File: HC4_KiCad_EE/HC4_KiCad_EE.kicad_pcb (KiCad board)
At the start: 2 copper layers, 100 x 100 mm, 124 parts, among them IC1 74HC86, IC10 74HC161, IC11 74HC02, IC12 74HC00, IC13 74HC4053, IC14 74HC74, IC15 74HC14, IC2 74HC283, IC3 74HC253, IC4 74HC253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

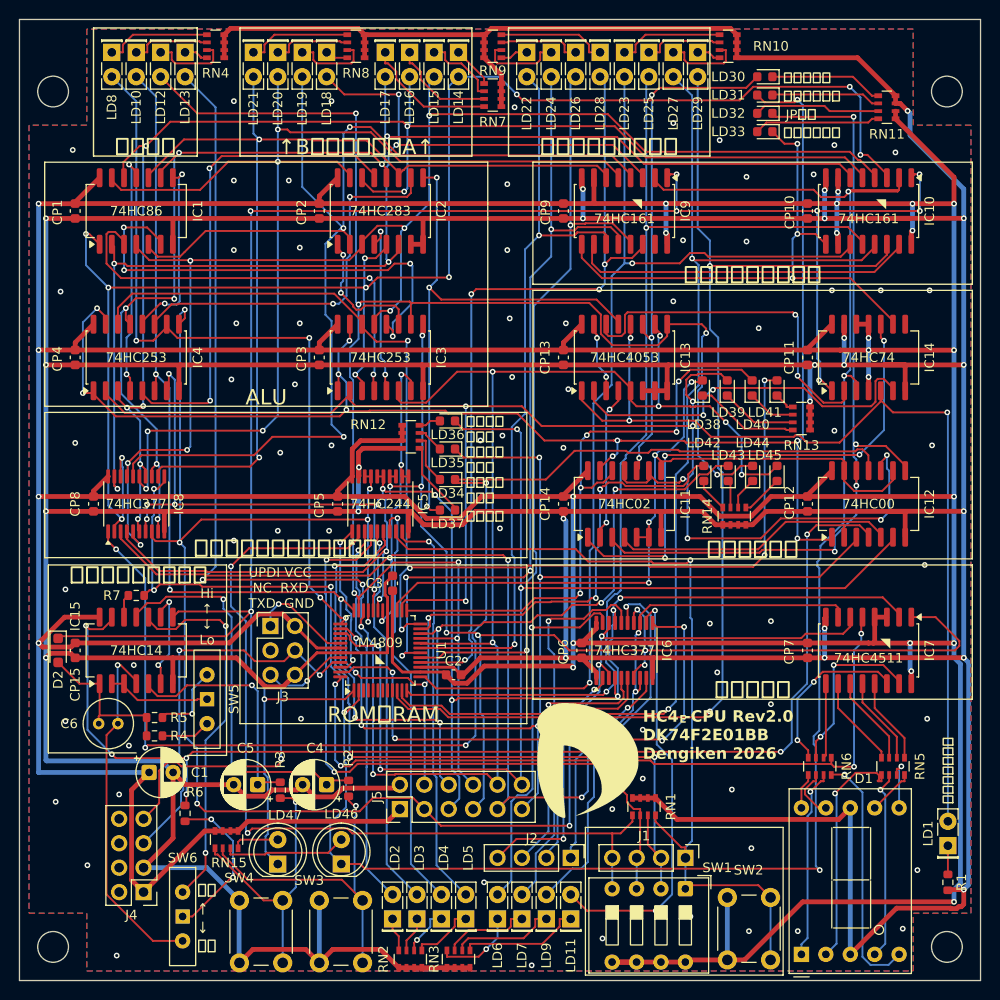
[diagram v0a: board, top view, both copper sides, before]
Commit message: 基板を若干改版、フットプリントの指定が外れていたのを修正
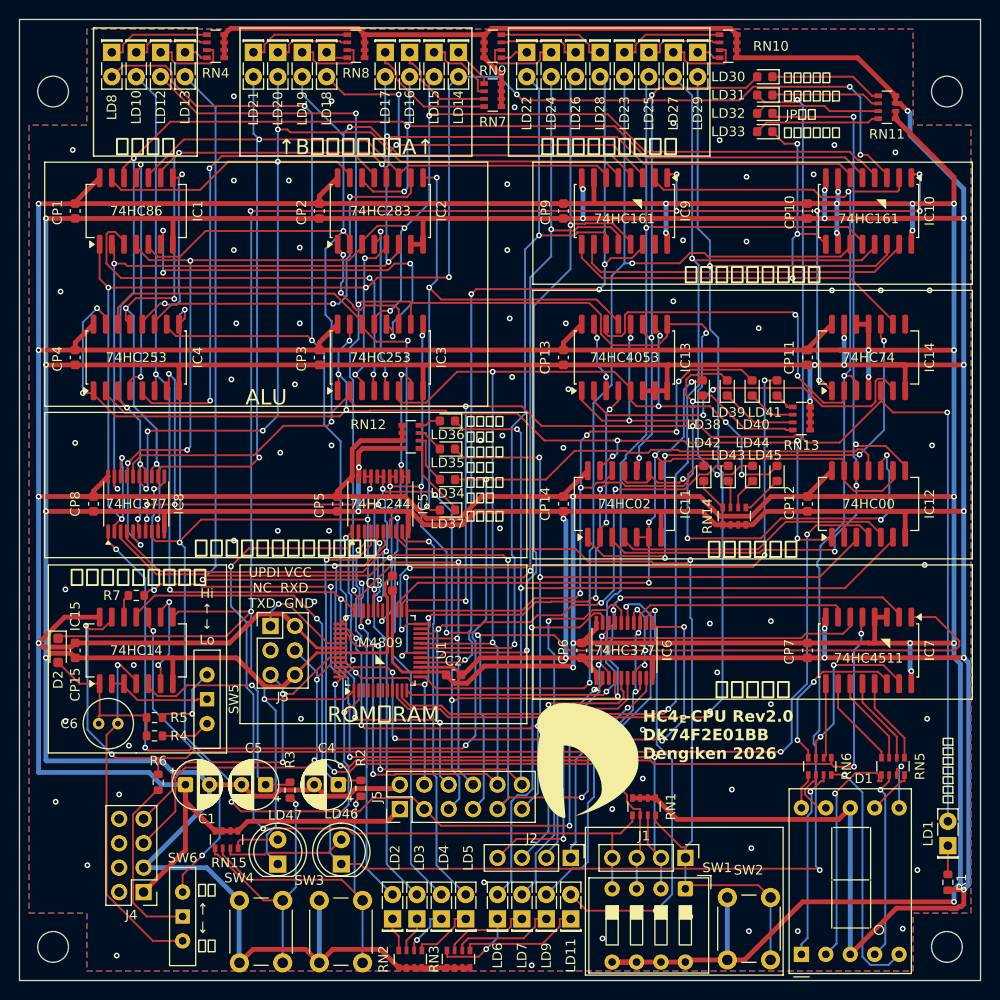
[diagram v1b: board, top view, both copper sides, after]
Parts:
- moved R6 4.28 mm to (59.4, 134.4)
- moved C1 3.99 mm to (62.3, 134.6)
- moved R2 1.27 mm to (80.5, 135.0)
- moved C4 1.21 mm to (78.2, 134.6)
- moved R3 1.02 mm to (73.2, 135.2)
- moved C5 0.83 mm to (70.6, 134.6)
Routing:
- net /ALU/Instruction_3: track 155.4 -> 170.4 mm, vias 9 -> 8
- net /ALU/ALU_in_B1: track 131.8 -> 119.0 mm
- net /ALU/XOR1: track 49.3 -> 42.1 mm
- net Net-(SW6-C): track 38.9 -> 33.3 mm
- net CLK: track 225.1 -> 220.1 mm
- net /ALU/ALU_in_A0: track 171.9 -> 168.3 mm, vias 11 -> 10
- net CLK2: track 125.7 -> 122.3 mm, vias 6 -> 4
- net /Instruction Decoder/~{STACK_LE}: track 135.9 -> 133.1 mm
- net /ALU/ALU_in_A2: track 146.4 -> 144.0 mm, vias 7 -> 6
- net /ALU/ALU_OUT3: track 188.7 -> 186.5 mm
- net /ROM_RAM/RX: track 41.2 -> 39.2 mm
- net Net-(SW6-B): track 16.7 -> 18.6 mm, vias 2 -> 0
- net Net-(IC5-1A0): track 91.0 -> 89.4 mm
- net Net-(RN15A-R1.1): track 28.8 -> 27.5 mm
- net /ROM_RAM/TX: track 36.0 -> 35.0 mm
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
